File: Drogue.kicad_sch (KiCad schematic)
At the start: 7 parts, among them J1 Pyro, Q1 BSC098N10NS5, Q3 NMOS

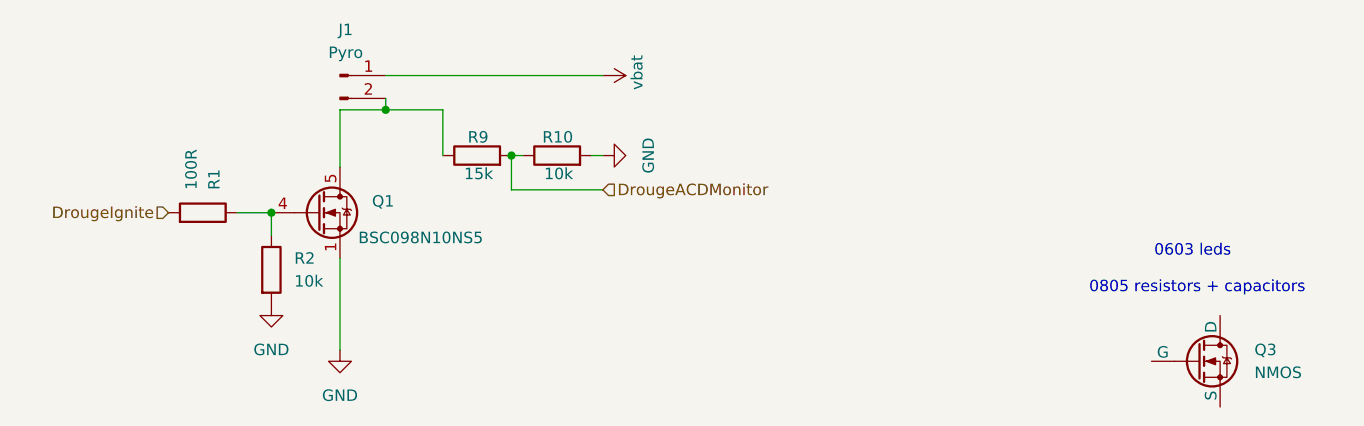
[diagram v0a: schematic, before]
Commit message: began fixing schematic added barometer
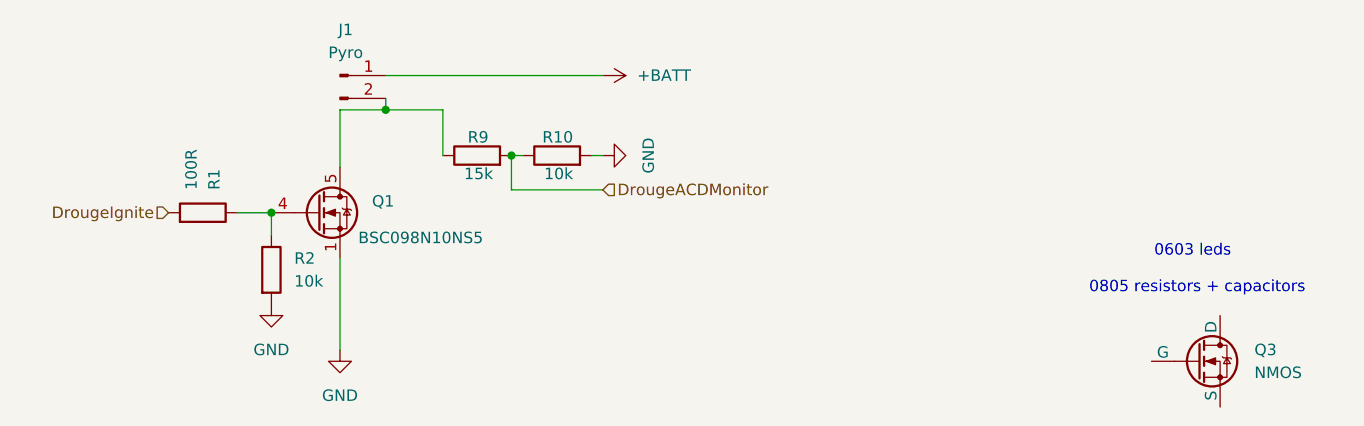
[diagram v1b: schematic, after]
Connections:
- net vbat renamed +BATT
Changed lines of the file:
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@@
+	)
+	(symbol
+		(lib_id "power:+BATT")
+		(at 160.02 60.96 270)
+		(unit 1)
+		(exclude_from_sim no)
+		(in_bom yes)
+		(on_board yes)
+		(dnp no)
+		(fields_autoplaced yes)
+		(property "Reference" "#PWR03"
+			(at 156.21 60.96 0)
+			(effects
+				(font
+					(size 1.27 1.27)
+				)
+				(hide yes)
+			)
+		)
+		(property "Value" "+BATT"
+			(at 163.83 60.9599 90)
+			(effects
+				(font
+					(size 1.27 1.27)
+				)
+				(justify left)
+			)
+		)
+		(property "Footprint" ""
+			(at 160.02 60.96 0)
+			(effects
+				(font
+					(size 1.27 1.27)
+				)
+				(hide yes)
+			)
+		)
+		(property "Datasheet" ""
+			(at 160.02 60.96 0)
+			(effects
+				(font
+					(size 1.27 1.27)
+				)
+				(hide yes)
+			)
+		)
+		(property "Description" "Power symbol creates a global label with name \"+BATT\""
+			(at 160.02 60.96 0)
+			(effects
+				(font
+					(size 1.27 1.27)
+				)
+				(hide yes)
+			)
+		)
+		(pin "1"
+		)
+		(instances
+			(project ""
+				(path "/6cb3dda3-5fe8-4715-b831-354360aa3199/49edfe84-9da0-4fce-8baf-f24126c92814"
+					(reference "#PWR03")
+					(unit 1)
+				)
+			)
+		)
 	)
 	(symbol
@@
 					(unit 1)
 				)
-			)
-		)
-	)
-	(symbol
-		(lib_id "power:+7.5V")
-		(at 160.02 60.96 270)
-		(unit 1)
-		(exclude_from_sim no)
-		(in_bom yes)
-		(on_board yes)
-		(dnp no)
-		(property "Reference" "#PWR03"
-			(at 156.21 60.96 0)
-			(effects
-				(font
-					(size 1.27 1.27)
-				)
-				(hide yes)
-			)
-		)
-		(property "Value" "vbat"
-			(at 163.83 58.674 0)
-			(effects
-				(font
-					(size 1.27 1.27)
-				)
-				(justify left)
-			)
-		)
-		(property "Footprint" ""
-			(at 160.02 60.96 0)
-			(effects
-				(font
-					(size 1.27 1.27)
-				)
-				(hide yes)
-			)
-		)
-		(property "Datasheet" ""
-			(at 160.02 60.96 0)
-			(effects
-				(font
-					(size 1.27 1.27)
-				)
-				(hide yes)
-			)
-		)
-		(property "Description" "Power symbol creates a global label with name \"+7.5V\""
-			(at 160.02 60.96 0)
-			(effects
-				(font
-					(size 1.27 1.27)
-				)
-				(hide yes)
-			)
-		)
-		(pin "1"
-		)
-		(instances
-			(project "flightcomputer2"
-				(path "/6cb3dda3-5fe8-4715-b831-354360aa3199/49edfe84-9da0-4fce-8baf-f24126c92814"
-					(reference "#PWR03")
-					(unit 1)
-				)
